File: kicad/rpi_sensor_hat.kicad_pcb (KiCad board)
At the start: 2 copper layers, 1 part, among them J1 SSW-120-03-G-D

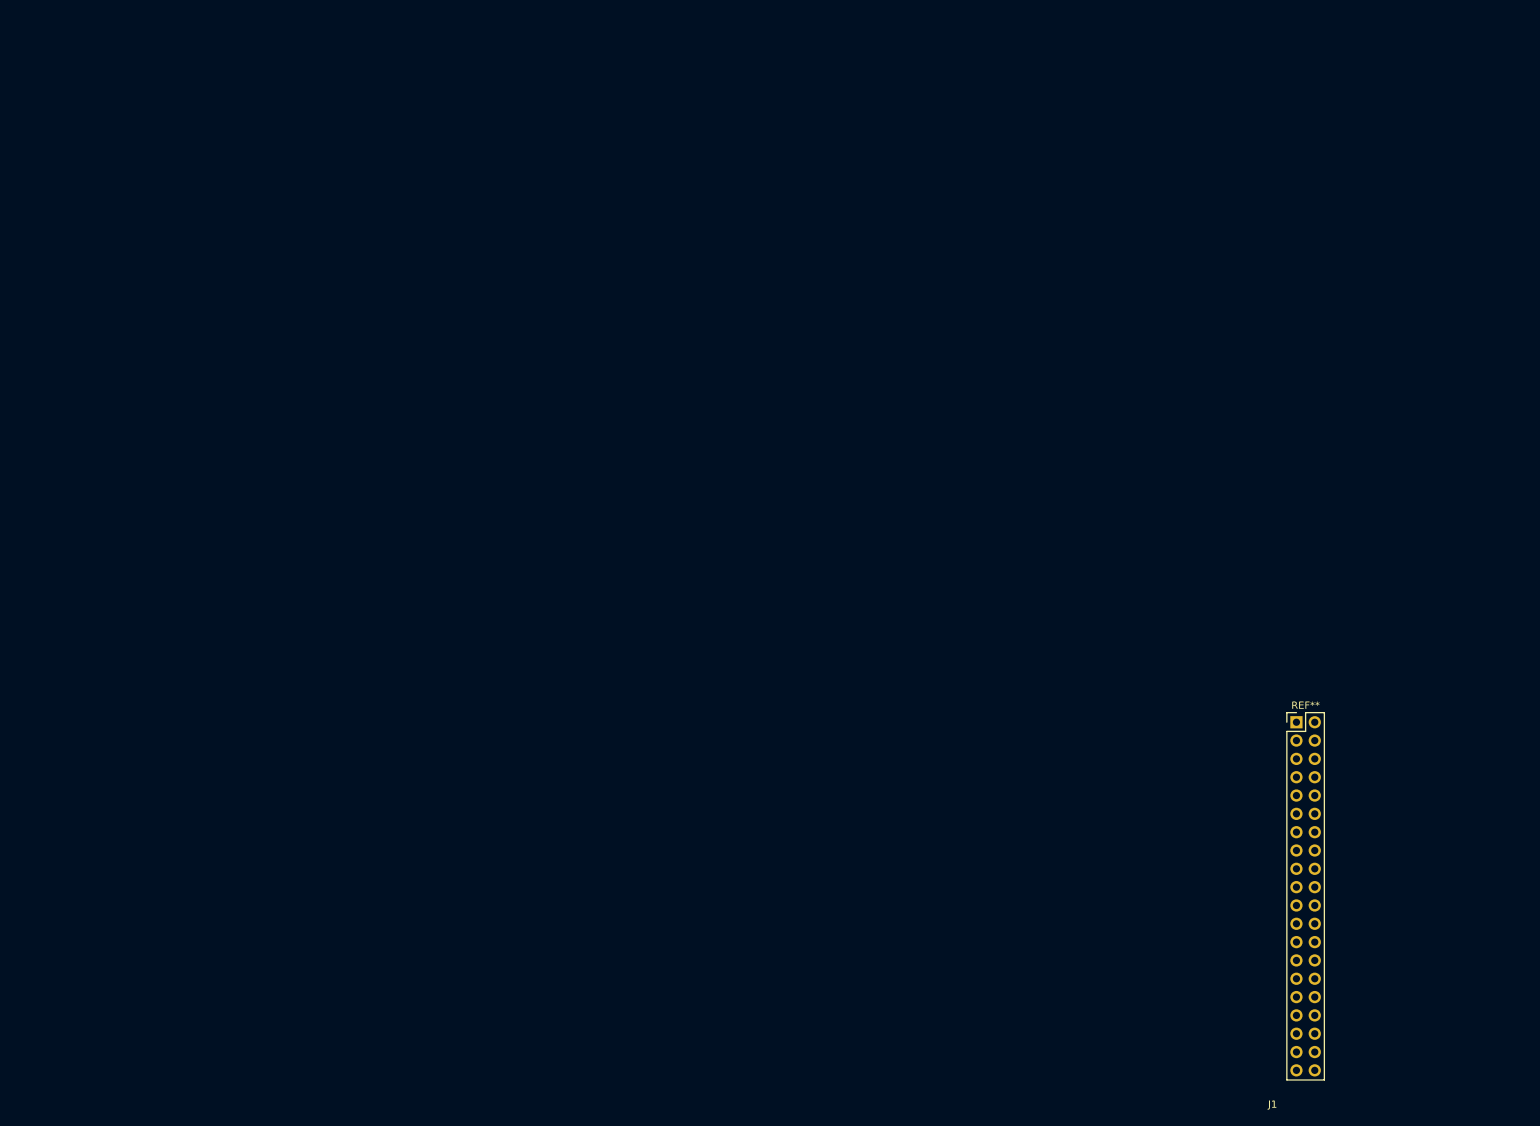
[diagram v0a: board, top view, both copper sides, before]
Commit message: Added battery and power management.
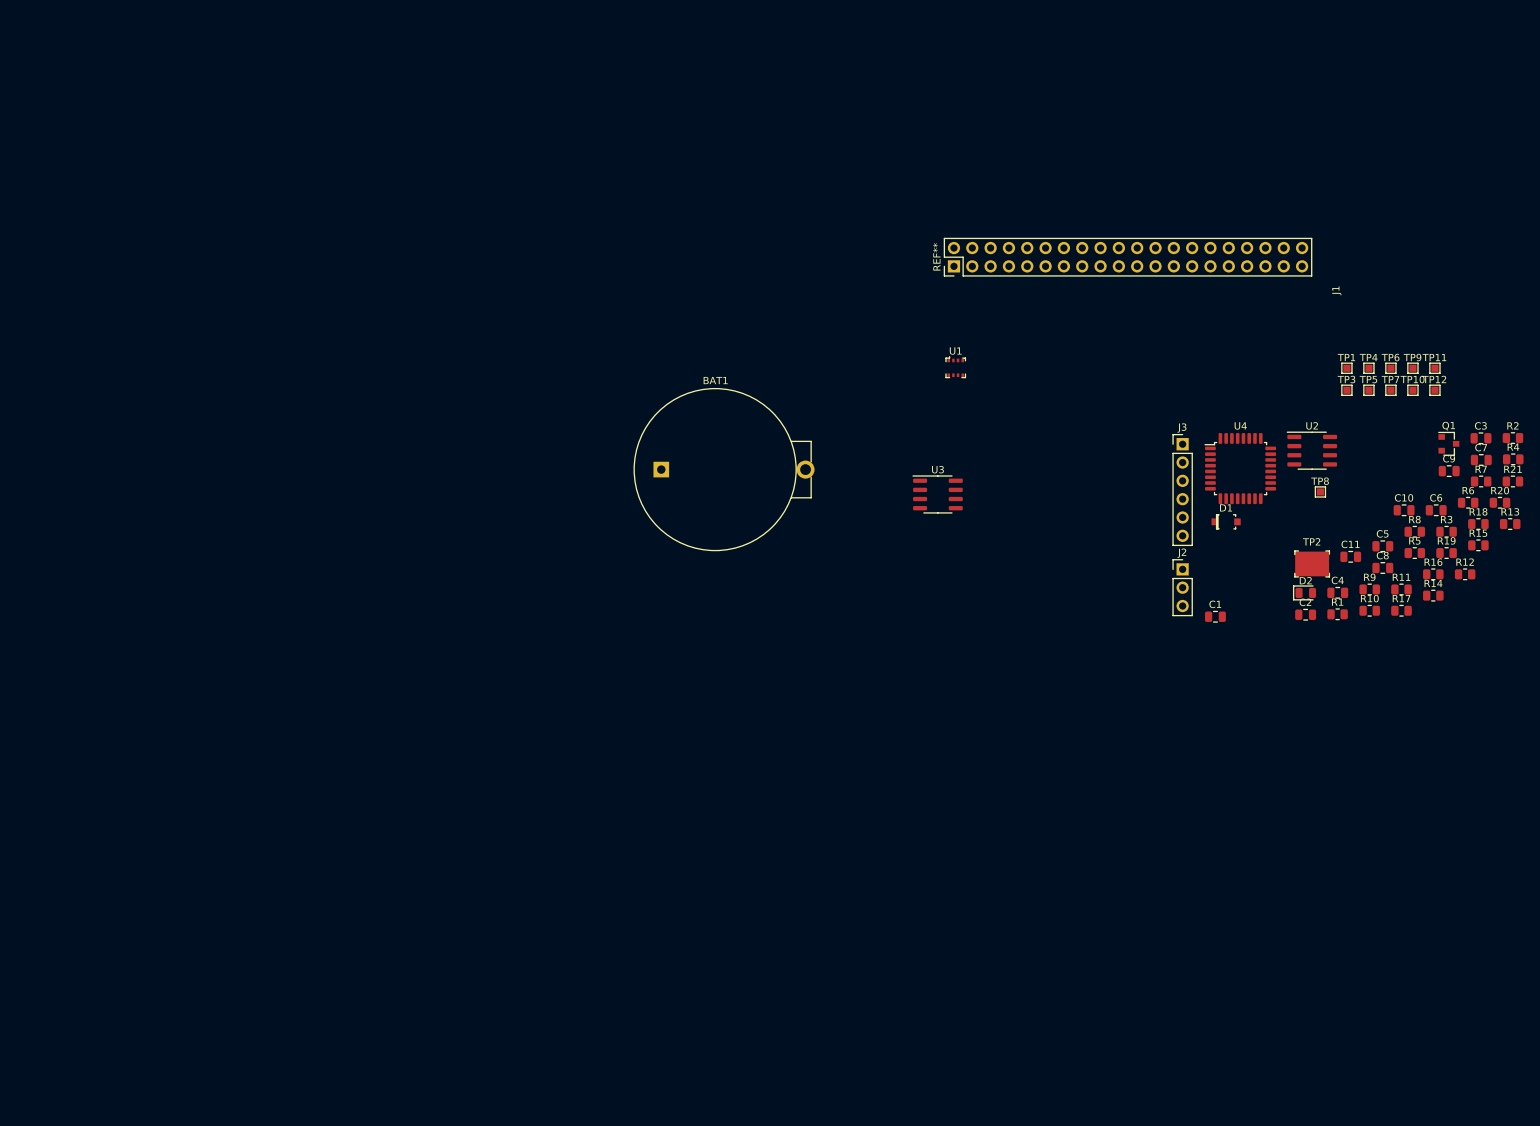
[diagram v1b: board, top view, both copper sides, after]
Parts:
- added BAT1: BS-7, rpi_sensor_hat:Battery_Holder_Coin_2032_BS-7, F.Cu at (139.6, 113.0)
- added C1: 10uF, Capacitor_SMD:C_0805_2012Metric, F.Cu at (216.4, 133.4)
- added C10: 0.1uF, Capacitor_SMD:C_0805_2012Metric, F.Cu at (242.5, 118.6)
- added C11: 0.1uF, Capacitor_SMD:C_0805_2012Metric, F.Cu at (235.1, 125.1)
- added C2: 0.1uF, Capacitor_SMD:C_0805_2012Metric, F.Cu at (228.9, 133.1)
- added C3: 0.1uF, Capacitor_SMD:C_0805_2012Metric, F.Cu at (253.2, 108.6)
- added C4: 0.1uF, Capacitor_SMD:C_0805_2012Metric, F.Cu at (233.3, 130.1)
- added C5: 0.1uF, Capacitor_SMD:C_0805_2012Metric, F.Cu at (239.6, 123.6)
- added C6: 0.1uF, Capacitor_SMD:C_0805_2012Metric, F.Cu at (247.0, 118.6)
- added C7: 0.1uF, Capacitor_SMD:C_0805_2012Metric, F.Cu at (253.2, 111.6)
- added C8: 0.1uF, Capacitor_SMD:C_0805_2012Metric, F.Cu at (239.6, 126.6)
- added C9: 0.1uF, Capacitor_SMD:C_0805_2012Metric, F.Cu at (248.8, 113.2)
- added D1: MBR0520LT1G, rpi_sensor_hat:SOD-123, F.Cu at (217.8, 120.2)
- added D2: LG_R971-KN-1, LED_SMD:LED_0805_2012Metric, F.Cu at (228.9, 130.1)
- added J2: Conn_01x03, Connector_PinHeader_2.54mm:PinHeader_1x03_P2.54mm_Vertical, F.Cu at (211.8, 126.8)
- added J3: Conn_01x06, Connector_PinHeader_2.54mm:PinHeader_1x06_P2.54mm_Vertical, F.Cu at (211.8, 109.5)
- added Q1: BSS84, Package_TO_SOT_SMD:SOT-23, F.Cu at (248.7, 109.4)
- added R1: 100K, Resistor_SMD:R_0805_2012Metric, F.Cu at (233.3, 133.0)
- added R10: 10K, Resistor_SMD:R_0805_2012Metric, F.Cu at (237.8, 132.5)
- added R11: 10K, Resistor_SMD:R_0805_2012Metric, F.Cu at (242.2, 129.6)
- added R12: 10K, Resistor_SMD:R_0805_2012Metric, F.Cu at (251.0, 127.5)
- added R13: 10K, Resistor_SMD:R_0805_2012Metric, F.Cu at (257.2, 120.5)
- added R14: 100R, Resistor_SMD:R_0805_2012Metric, F.Cu at (246.6, 130.4)
- added R15: 100R, Resistor_SMD:R_0805_2012Metric, F.Cu at (252.8, 123.5)
- added R16: 3.9K, Resistor_SMD:R_0805_2012Metric, F.Cu at (246.6, 127.5)
- added R17: 3.9K, Resistor_SMD:R_0805_2012Metric, F.Cu at (242.2, 132.5)
- added R18: 100R, Resistor_SMD:R_0805_2012Metric, F.Cu at (252.8, 120.5)
- added R19: 10K, Resistor_SMD:R_0805_2012Metric, F.Cu at (248.4, 124.5)
- added R2: 1K, Resistor_SMD:R_0805_2012Metric, F.Cu at (257.6, 108.6)
- added R20: 100R, Resistor_SMD:R_0805_2012Metric, F.Cu at (255.8, 117.6)
- added R21: 100R, Resistor_SMD:R_0805_2012Metric, F.Cu at (257.6, 114.6)
- added R3: 3.9K, Resistor_SMD:R_0805_2012Metric, F.Cu at (248.4, 121.6)
- added R4: 3.9K, Resistor_SMD:R_0805_2012Metric, F.Cu at (257.7, 111.6)
- added R5: 100R, Resistor_SMD:R_0805_2012Metric, F.Cu at (244.0, 124.5)
- added R6: 100R, Resistor_SMD:R_0805_2012Metric, F.Cu at (251.4, 117.6)
- added R7: 10K, Resistor_SMD:R_0805_2012Metric, F.Cu at (253.2, 114.6)
- added R8: 10K, Resistor_SMD:R_0805_2012Metric, F.Cu at (244.0, 121.6)
- added R9: 10K, Resistor_SMD:R_0805_2012Metric, F.Cu at (237.8, 129.6)
- added TP1: 5016, TestPoint:TestPoint_Pad_1.0x1.0mm, F.Cu at (234.6, 98.9)
- added TP10: 5016, TestPoint:TestPoint_Pad_1.0x1.0mm, F.Cu at (243.8, 102.0)
- added TP11: 5016, TestPoint:TestPoint_Pad_1.0x1.0mm, F.Cu at (246.8, 98.9)
- added TP12: 5016, TestPoint:TestPoint_Pad_1.0x1.0mm, F.Cu at (246.8, 102.0)
- added TP2: 5016, digikey-footprints:Test_Point_3.43x1.78mm, F.Cu at (229.8, 126.1)
- added TP3: 5016, TestPoint:TestPoint_Pad_1.0x1.0mm, F.Cu at (234.6, 102.0)
- added TP4: 5016, TestPoint:TestPoint_Pad_1.0x1.0mm, F.Cu at (237.7, 98.9)
- added TP5: 5016, TestPoint:TestPoint_Pad_1.0x1.0mm, F.Cu at (237.7, 102.0)
- added TP6: 5016, TestPoint:TestPoint_Pad_1.0x1.0mm, F.Cu at (240.7, 98.9)
- added TP7: 5016, TestPoint:TestPoint_Pad_1.0x1.0mm, F.Cu at (240.7, 102.0)
- added TP8: 5016, TestPoint:TestPoint_Pad_1.0x1.0mm, F.Cu at (230.9, 116.1)
- added TP9: 5016, TestPoint:TestPoint_Pad_1.0x1.0mm, F.Cu at (243.8, 98.9)
- added U1: BME280, rpi_sensor_hat:Pressure_Sensor_LGA-8_2.5x2.5mm_BME280, F.Cu at (180.4, 98.9)
- added U2: CAT24C128, Package_SO:SOIC-8_3.9x4.9mm_P1.27mm, F.Cu at (229.8, 110.4)
- added U3: FM25V10-G, Package_SO:SOIC-8_3.9x4.9mm_P1.27mm, F.Cu at (177.9, 116.4)
- added U4: STM32L062K8Tx, Package_QFP:LQFP-32_7x7mm_P0.8mm, F.Cu at (219.9, 112.8)
- moved J1 112.7 mm to (232.6, 88.1), turned to 90 degrees
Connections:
- net Net-(J1-Pad11) renamed /GPIO17
- net Net-(J1-Pad12) renamed /GPIO18_PCM_CLK
- net Net-(J1-Pad13) renamed /GPIO27
- net Net-(J1-Pad15) renamed /GPIO22
- net Net-(J1-Pad16) renamed /GPIO23
- net Net-(J1-Pad18) renamed /GPIO24
- net Net-(J1-Pad19) renamed /GPIO10_MOSI
- net Net-(J1-Pad21) renamed /GPIO9_MISO
- net Net-(J1-Pad22) renamed /GPIO25
- net Net-(J1-Pad23) renamed /GPIO11_SCLK
- net Net-(J1-Pad24) renamed /GPIO8_CE0
- net Net-(J1-Pad26) renamed /GPIO7_CE1
- net Net-(J1-Pad29) renamed /GPIO5
- net Net-(J1-Pad31) renamed /GPIO6
- net Net-(J1-Pad32) renamed /GPIO12_PWM0
- net Net-(J1-Pad33) renamed /GPIO13_PWM1
- net Net-(J1-Pad35) renamed /GPIO19_PCM_FS
- net Net-(J1-Pad36) renamed /GPIO16
- net Net-(J1-Pad37) renamed /GPIO26
- net Net-(J1-Pad38) renamed /GPIO20_PCM_DIN
- net Net-(J1-Pad40) renamed /GPIO21_PCM_DOUT
- net Net-(J1-Pad7) renamed /GPIO4_GPCLK0
- J1 pad 1: Net-(J1-Pad1) -> +3.3VP
- J1 pad 10: Net-(J1-Pad10) -> /GPIO15_RXD
- J1 pad 14: Net-(J1-Pad14) -> GND
- J1 pad 17: Net-(J1-Pad17) -> +3.3VP
- J1 pad 20: Net-(J1-Pad20) -> GND
- J1 pad 25: Net-(J1-Pad25) -> GND
- J1 pad 27: Net-(J1-Pad27) -> /GPIO0_ID_SD
- J1 pad 28: Net-(J1-Pad28) -> /GPIO1_ID_SC
- J1 pad 3: Net-(J1-Pad3) -> /GPIO2_SDA
- J1 pad 30: Net-(J1-Pad30) -> GND
- J1 pad 34: Net-(J1-Pad34) -> GND
- J1 pad 39: Net-(J1-Pad39) -> GND
- J1 pad 5: Net-(J1-Pad5) -> /GPIO3_SCL
- J1 pad 6: Net-(J1-Pad6) -> GND
- J1 pad 8: Net-(J1-Pad8) -> /GPIO14_TXD
- J1 pad 9: Net-(J1-Pad9) -> GND

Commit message: Completed rev 0 of PCB layout.
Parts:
- removed C11: 0.1uF, Capacitor_SMD:C_0805_2012Metric
- removed TP11, TP12: 5016, TestPoint:TestPoint_Pad_1.0x1.0mm
- added D3: LG_R971-KN-1, LED_SMD:LED_0805_2012Metric, F.Cu at (58.0, 79.0)
- added D4: LG_R971-KN-1, LED_SMD:LED_0805_2012Metric, F.Cu at (58.0, 83.5)
- added H1: MountingHole, MountingHole:MountingHole_2.7mm_M2.5, F.Cu at (111.5, 53.8)
- added H2: MountingHole, MountingHole:MountingHole_2.7mm_M2.5, F.Cu at (53.5, 102.8)
- added H3: MountingHole, MountingHole:MountingHole_2.7mm_M2.5, F.Cu at (111.5, 102.8)
- added H4: MountingHole, MountingHole:MountingHole_2.7mm_M2.5, F.Cu at (53.5, 53.8)
- added J4: Conn_01x03, Connector_PinHeader_2.54mm:PinHeader_1x03_P2.54mm_Vertical, F.Cu at (113.0, 70.2)
- added J5: Conn_02x05_Odd_Even, Connector_PinHeader_1.27mm:PinHeader_2x05_P1.27mm_Vertical_SMD, F.Cu at (97.4, 82.9)
- added R22: 10K, Resistor_SMD:R_0805_2012Metric, F.Cu at (107.3, 96.8)
- added R23: 10K, Resistor_SMD:R_0805_2012Metric, F.Cu at (101.1, 96.8)
- added R24: 10K, Resistor_SMD:R_0805_2012Metric, F.Cu at (77.6, 84.3)
- added R25: 100R, Resistor_SMD:R_0805_2012Metric, F.Cu at (62.0, 79.0)
- added R26: 100R, Resistor_SMD:R_0805_2012Metric, F.Cu at (62.0, 83.5)
- added R27: 100R, Resistor_SMD:R_0805_2012Metric, F.Cu at (73.3, 84.3)
- added R28: 10K, Resistor_SMD:R_0805_2012Metric, F.Cu at (62.1, 71.0)
- added REF**: KiCad-Logo2_5mm_SilkScreen, Symbol:KiCad-Logo2_5mm_SilkScreen, F.Cu at (53.4, 93.4)
- added REF**: Symbol_CreativeCommonsPublicDomain_SilkScreenTop_Small, Symbol:Symbol_CreativeCommonsPublicDomain_SilkScreenTop_Small, F.Cu at (81.4, 101.3)
- J1: moved to B.Cu
- R14: value 100R -> 10K
- R19: value 10K -> 100R
- TP2: footprint digikey-footprints:Test_Point_3.43x1.78mm -> TestPoint:TestPoint_Pad_1.0x1.0mm
- moved R15 197.0 mm to (62.0, 74.5), turned to 180 degrees
- moved R7 193.8 mm to (60.5, 93.9), turned to 270 degrees
- moved R21 190.9 mm to (69.2, 84.3), turned to 270 degrees
- moved R1 190.0 mm to (58.5, 58.5), turned to 180 degrees
- moved Q1 189.8 mm to (65.5, 60.0)
- moved C6 188.6 mm to (60.5, 90.2), turned to 90 degrees
- moved R20 187.6 mm to (71.2, 84.3), turned to 270 degrees
- moved R16 186.6 mm to (65.0, 84.3), turned to 90 degrees
- moved TP1 186.2 mm to (52.5, 60.0)
- moved C2 183.5 mm to (58.5, 65.0), turned to 180 degrees
- moved R17 181.6 mm to (67.1, 84.3), turned to 90 degrees
- moved D2 179.7 mm to (58.0, 74.5)
- moved C7 175.6 mm to (79.8, 84.3), turned to 90 degrees
- moved R2 175.2 mm to (89.7, 58.7), turned to 270 degrees
- moved TP2 173.9 mm to (68.9, 60.0)
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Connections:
- C10 pad 1: Net-(C10-Pad1) -> /NRST
- C10 pad 2: Net-(C10-Pad2) -> GND
- C3 pad 1: +3V3 -> +3.3VP
- J1 pad 11: /GPIO17 -> /GPIO17_LED
- J1 pad 13: /GPIO27 -> /GPIO27_IRQ
- R11 pad 2: /FRAM_CS -> Net-(J4-Pad3)
- R12 pad 1: +3V3 -> Net-(J4-Pad1)
- R12 pad 2: /FRAM_~WP -> GND
- R13 pad 2: /FRAM_~HOLD -> /REV_BIT1
- R14 pad 1: Net-(R14-Pad1) -> /REV_BIT1
- R14 pad 2: Net-(R14-Pad2) -> GND
- R18 pad 1: Net-(R18-Pad1) -> /SWDIO
- R19 pad 1: Net-(R19-Pad1) -> /SWCLK
- R7 pad 2: /STM32_SCK -> /FRAM_CS
- R8 pad 2: /STM32_MOSI -> /REV_BIT0
- R9 pad 1: +3V3 -> /REV_BIT0
- R9 pad 2: /STM32_MISO -> GND
- U4 pad 10: Net-(U4-Pad10) -> /FRAM_CS
- U4 pad 11: Net-(U4-Pad11) -> /STM32_SCK
- U4 pad 12: Net-(U4-Pad12) -> /STM32_MISO
- U4 pad 13: Net-(U4-Pad13) -> /STM32_MOSI
- U4 pad 14: Net-(U4-Pad14) -> /REV_BIT0
- U4 pad 15: Net-(U4-Pad15) -> /REV_BIT1
- U4 pad 18: Net-(U4-Pad18) -> /SENSOR_CS
- U4 pad 21: Net-(U4-Pad21) -> /FRAM_~WP
- U4 pad 22: Net-(U4-Pad22) -> /FRAM_~HOLD
- U4 pad 23: Net-(U4-Pad23) -> /SWDIO
- U4 pad 24: Net-(U4-Pad24) -> /SWCLK
- U4 pad 25: Net-(U4-Pad25) -> /STM32_LED
- U4 pad 26: Net-(U4-Pad26) -> /REV_BIT2
- U4 pad 27: Net-(U4-Pad27) -> +3.3VP
- U4 pad 4: Net-(U4-Pad4) -> /NRST
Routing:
- net +3.3VP: track 0.00 -> 113.5 mm, vias 0 -> 2
- net Net-(R21-Pad2): track 0.00 -> 62.0 mm, vias 0 -> 4
- net /GPIO2_SDA: track 0.00 -> 61.9 mm, vias 0 -> 1
- net /FRAM_~HOLD: track 0.00 -> 60.9 mm, vias 0 -> 4
- net Net-(R20-Pad2): track 0.00 -> 59.3 mm, vias 0 -> 4
- net GND: track 0.00 -> 58.1 mm, vias 0 -> 24
- net /REV_BIT2: track 0.00 -> 57.6 mm, vias 0 -> 6
- net /GPIO3_SCL: track 0.00 -> 57.2 mm, vias 0 -> 3
- net +3V3: track 0.00 -> 50.2 mm, vias 0 -> 20
- net /FRAM_~WP: track 0.00 -> 49.7 mm, vias 0 -> 4
- net /SENSOR_CS: track 0.00 -> 47.9 mm, vias 0 -> 4
- net /NRST: track 0.00 -> 47.7 mm, vias 0 -> 4
- net /USART2RX: track 0.00 -> 46.8 mm, vias 0 -> 4
- net /USART2TX: track 0.00 -> 43.3 mm, vias 0 -> 4
- net Net-(J4-Pad2): track 0.00 -> 41.2 mm, vias 0 -> 4
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- added copper zone on F.Cu, net +3V3
- added copper zone on In2.Cu, net +3V3
- added copper zone on F.Cu, net GND
- added copper zone on In1.Cu, net GND
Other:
- board outline added: 65 x 56.5 mm
- copper layers 2 -> 4
- board text added: "GND"
- board text added: "Jumper ID EEPROM 1-2: Read 2-3: Write"
- board text added: "Jumper STM32 1-2: FLASH 2-3: BOOT"
- board text added: "NC"
- board text added: "REV0"
- board text added: "RX"
- board text added: "SWD"
- board text added: "TX"
- board text added: "github.com/OberTechniks/rpi_sensor_hat"
